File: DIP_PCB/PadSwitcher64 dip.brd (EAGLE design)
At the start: 49.7 x 25.1 mm, 15 parts, among them U1 ATMEGA88A-PU

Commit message: Fixed component values on silkscreen.
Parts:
- R1: value 330 -> 330R
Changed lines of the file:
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@@
 <attribute name="VALUE" x="18.685" y="26.305" size="0.0254" layer="27" rot="R180"/>
 </element>
-<element name="R1" library="resistor" package="0207/10" value="330" x="20.32" y="17.78" smashed="yes" rot="R180">
+<element name="R1" library="resistor" package="0207/10" value="330R" x="20.32" y="17.78" smashed="yes" rot="R180">
 <attribute name="VALUE" x="22.5806" y="18.415" size="1.27" layer="25" ratio="10" rot="R180"/>
 </element>
@@
 </element>
 <element name="U1" library="Mine" package="DIL28-3" value="ATMEGA88A-PU" x="30.48" y="17.78" smashed="yes">
-<attribute name="VALUE" x="35.75685" y="19.05" size="1.1" layer="27" ratio="10" rot="SR0"/>
+<attribute name="VALUE" x="33.0581" y="17.30375" size="1.1" layer="25" ratio="10" rot="SR0"/>
 </element>
 </elements>

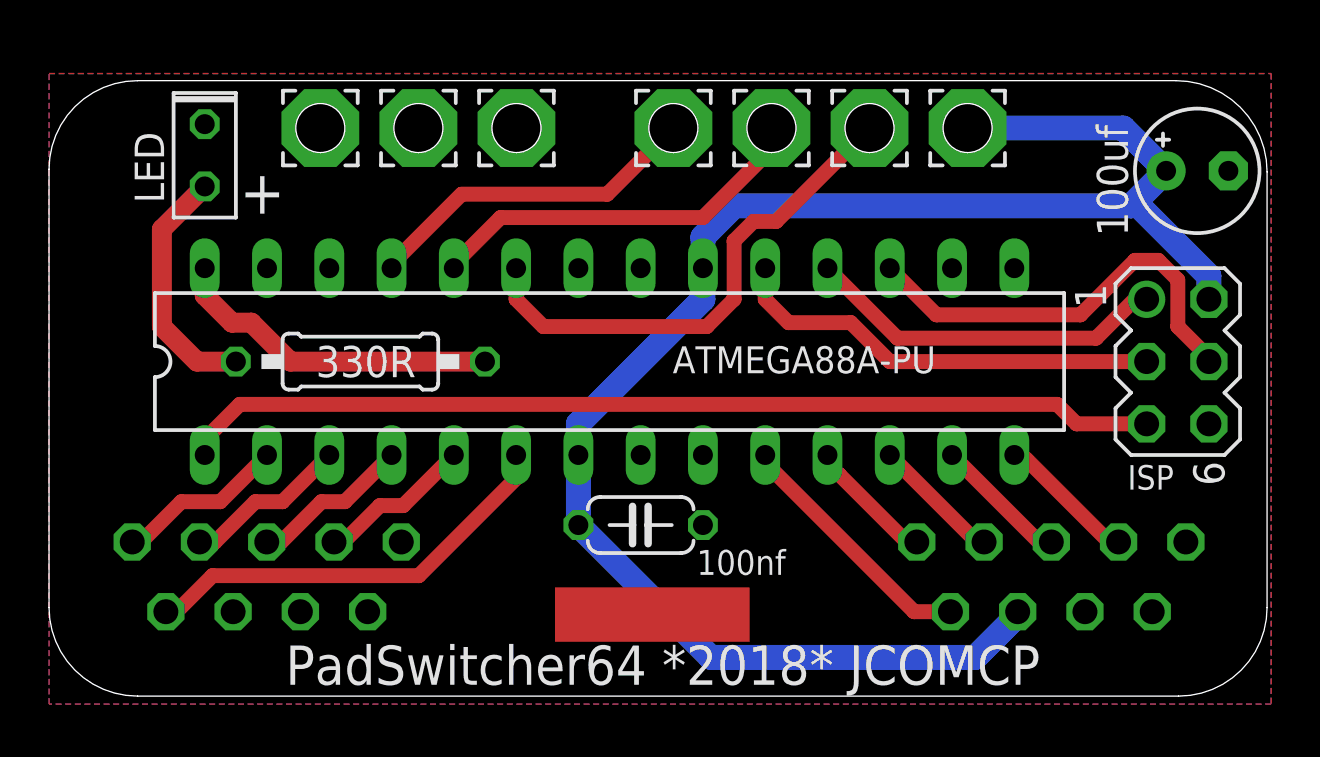
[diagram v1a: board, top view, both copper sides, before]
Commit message: Adjusted component positions.
Turns out that there wasn't enough room to mount the straight pin SNES socket properly.  The PCB has been enlarged a smidgen and the AVR and socket have been moved apart a little.
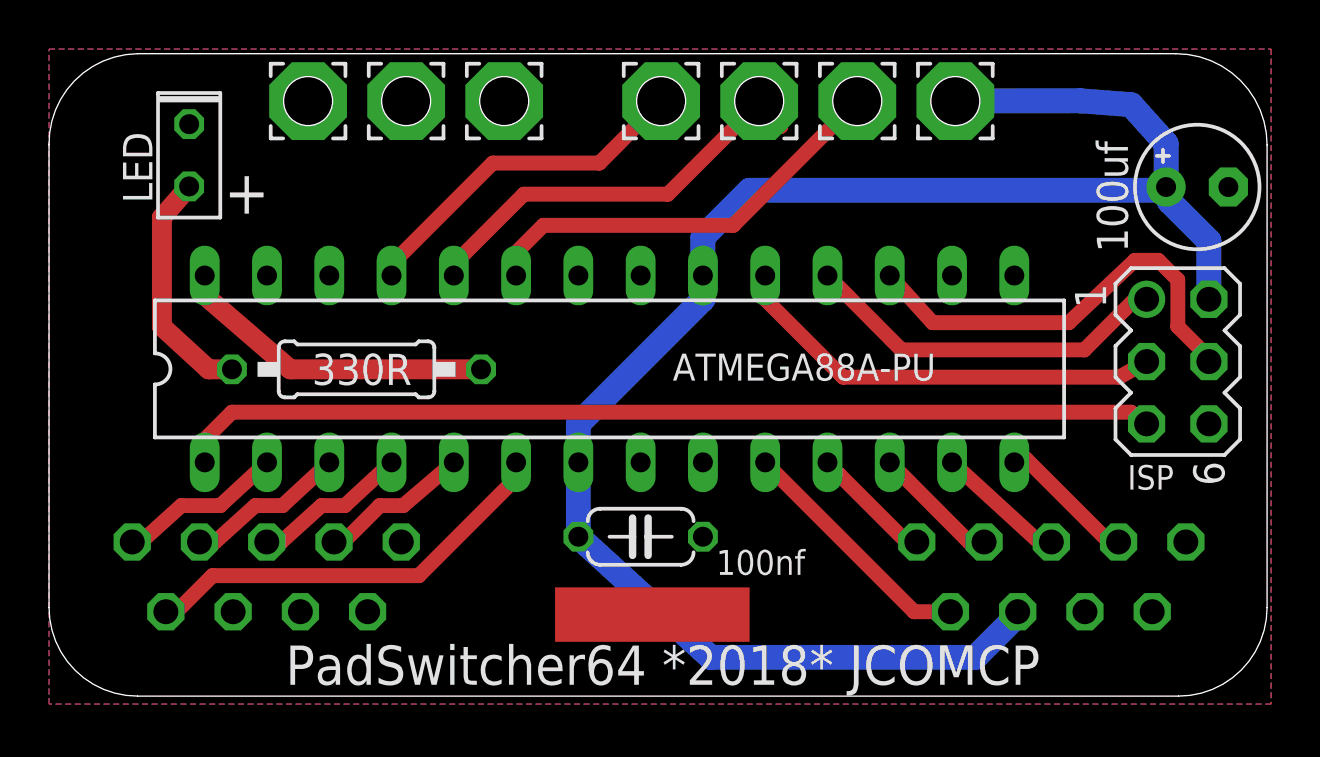
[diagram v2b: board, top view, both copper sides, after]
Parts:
- moved SNES_+5V 1.21 mm to (44.6, 28.4)
- moved SNES_CLK 1.21 mm to (40.6, 28.4)
- moved SNES_DATA_PAD1 1.21 mm to (32.6, 28.4)
- moved SNES_GND 1.21 mm to (18.2, 28.4)
- moved SNES_LATCH 1.21 mm to (36.6, 28.4)
- moved SNES_NC1 1.21 mm to (26.2, 28.4)
- moved SNES_NC2 1.21 mm to (22.2, 28.4)
- moved C2 0.66 mm to (54.5, 24.9)
- moved LED1 0.63 mm to (13.3, 26.2)
- moved C1 0.48 mm to (31.8, 10.6)
- moved R1 0.35 mm to (20.2, 17.5)
- moved U1 0.30 mm to (30.5, 17.5)
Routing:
- net N$15: track 20.9 -> 17.4 mm
- net +5V: track 69.4 -> 71.6 mm
- net N$16: track 15.9 -> 17.5 mm
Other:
- board size 49.7 x 25.1 mm -> 49.7 x 26.2 mm
- board text added: "This file is part of PadSwitcher64. PadSwitcher64 is free software / hardware: you can redistribute it and/or modify it under the terms of the GNU General Public License as published by the Free Software Foundation, either version 3 of the License, or (at your option) any later version. PadSwitcher64 is distributed in the hope that it will be useful, but WITHOUT ANY WARRANTY; without even the imp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"
- board text removed: "This file is part of PadSwitcher64. PadSwitcher64 is free software: you can redistribute it and/or modify it under the terms of the GNU General Public License as published by the Free Software Foundation, either version 3 of the License, or (at your option) any later version. PadSwitcher64 is distributed in the hope that it will be useful, but WITHOUT ANY WARRANTY; without even the implied warran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"

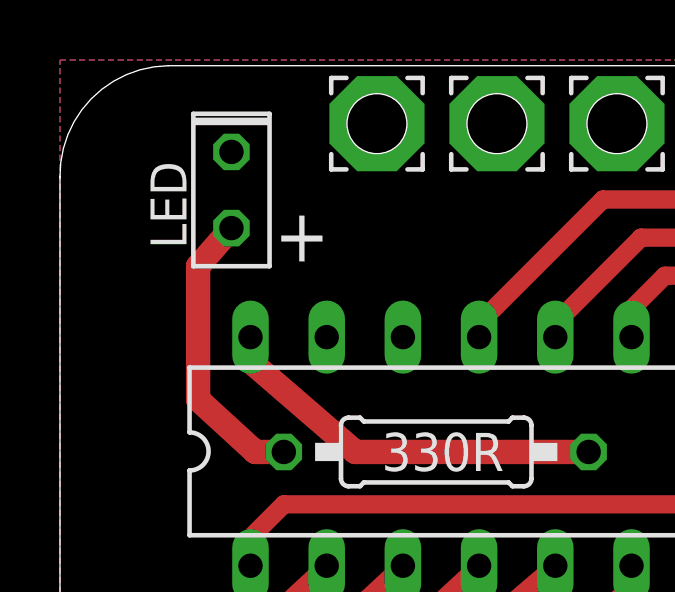
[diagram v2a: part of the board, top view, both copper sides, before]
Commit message: Adjusted component positions... again.
Forgot to nudge the LED out to the way a little.
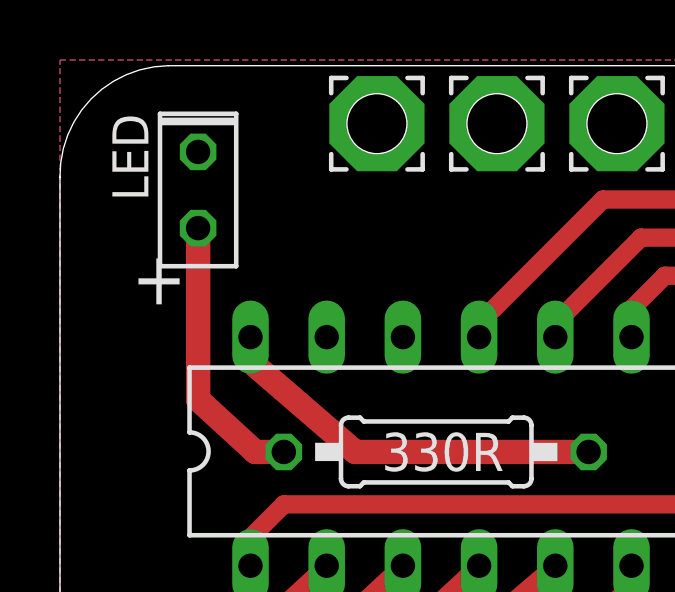
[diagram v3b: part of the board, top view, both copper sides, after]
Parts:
- moved LED1 1.11 mm to (12.2, 26.2)
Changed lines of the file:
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@@
 <wire x1="53.581378125" y1="30.3375" x2="11.2316" y2="30.3375" width="0" layer="20"/>
 <wire x1="11.2316" y1="30.3375" x2="7.62" y2="26.6259" width="0" layer="20" curve="90"/>
-<text x="14.76375" y="23.8125" size="1.778" layer="21">+</text>
+<text x="10.00125" y="22.38375" size="1.778" layer="21">+</text>
 <text x="32.65625" y="5.3975" size="1.6" layer="25" ratio="9" rot="R180" align="center">PadSwitcher64 *2018* JCOMCP</text>
-<text x="10.63625" y="27.14625" size="1.2" layer="25" rot="R270">LED</text>
+<text x="9.36625" y="28.73375" size="1.2" layer="25" rot="R270">LED</text>
 <text x="36.25" y="8.255" size="1.3" layer="29" ratio="12" rot="R180">REV. 5p</text>
 <hole x="44.585" y="28.405" drill="2"/>
@@
 <attribute name="VALUE" x="51.6255" y="22.233" size="1.27" layer="25" ratio="10" rot="R90"/>
 </element>
-<element name="LED1" library="led" package="LED2X5" value="" x="13.335" y="26.19375" smashed="yes" rot="R90">
-<attribute name="VALUE" x="17.78" y="26.82875" size="1.27" layer="27" ratio="10" rot="R90"/>
+<element name="LED1" library="led" package="LED2X5" value="" x="12.22375" y="26.19375" smashed="yes" rot="R90">
+<attribute name="VALUE" x="16.66875" y="26.82875" size="1.27" layer="27" ratio="10" rot="R90"/>
 </element>
 <element name="SNES_+5V" library="wirepad" package="3,17/1,1" value="" x="44.585" y="28.405" smashed="yes" rot="R180">
@@
 <wire x1="15.08125" y1="17.4625" x2="14.12875" y2="17.4625" width="0.8128" layer="1"/>
 <wire x1="14.12875" y1="17.4625" x2="12.22375" y2="19.20875" width="0.8128" layer="1"/>
-<wire x1="12.22375" y1="19.20875" x2="12.22375" y2="23.65375" width="0.8128" layer="1"/>
-<wire x1="12.22375" y1="23.65375" x2="13.335" y2="24.92375" width="0.8128" layer="1"/>
+<wire x1="12.22375" y1="19.20875" x2="12.22375" y2="24.92375" width="0.8128" layer="1"/>
 </signal>
 <signal name="N$1">
